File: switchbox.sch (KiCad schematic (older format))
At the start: 3 parts

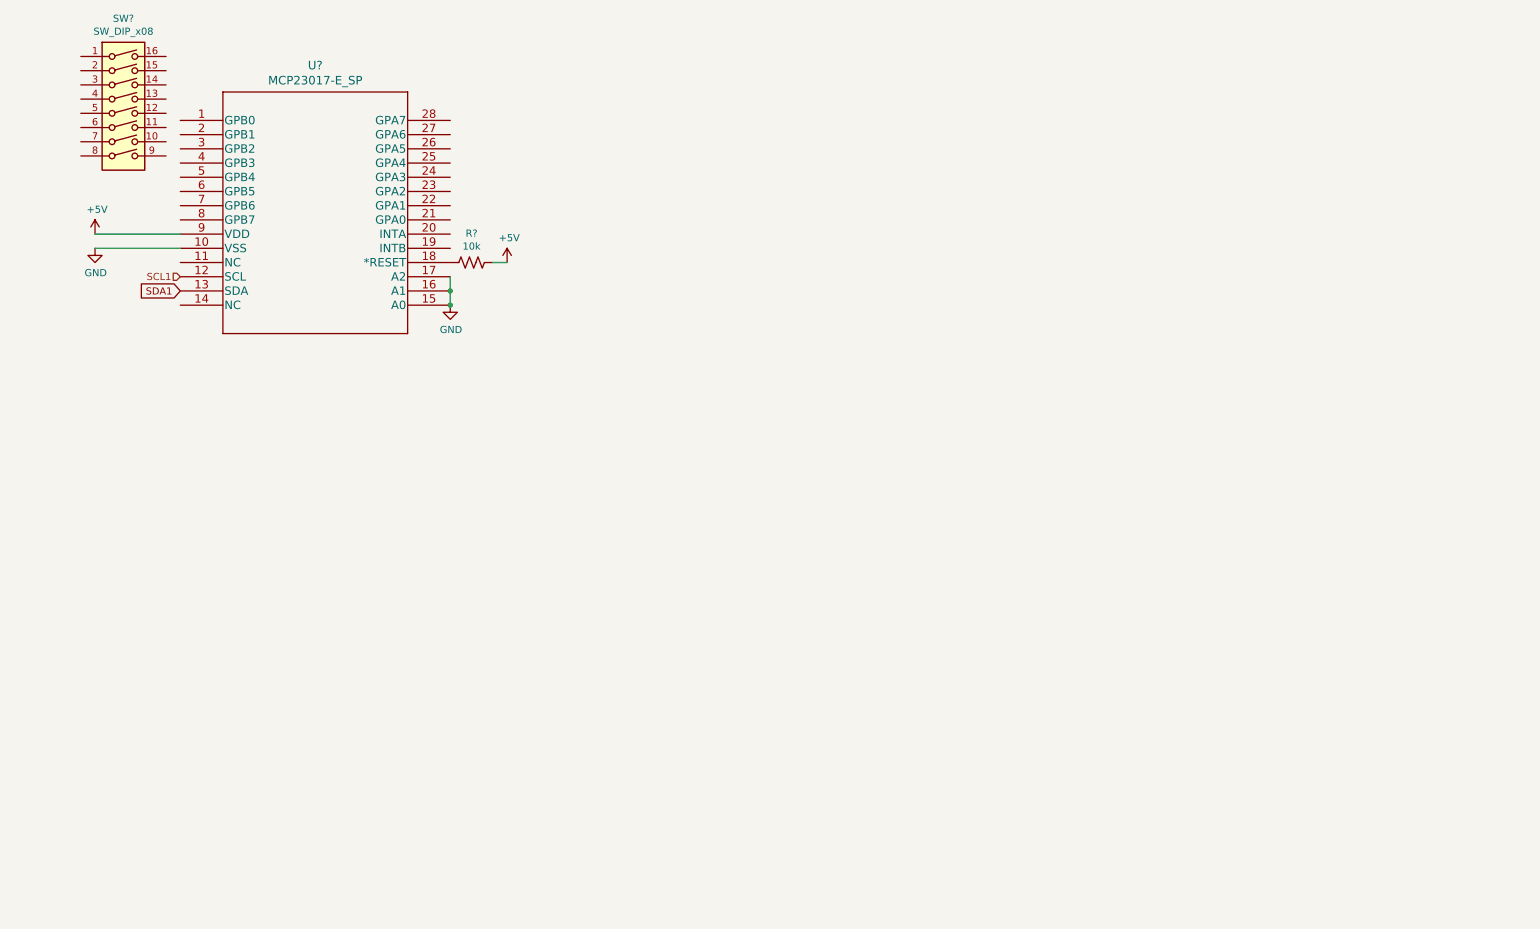
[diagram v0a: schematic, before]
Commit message: Switchbox Schematic Created
The nested schematic for the switchbox no exists using the 12V battery, LM2596 buck converter, and the MPC23017 I/O expander.
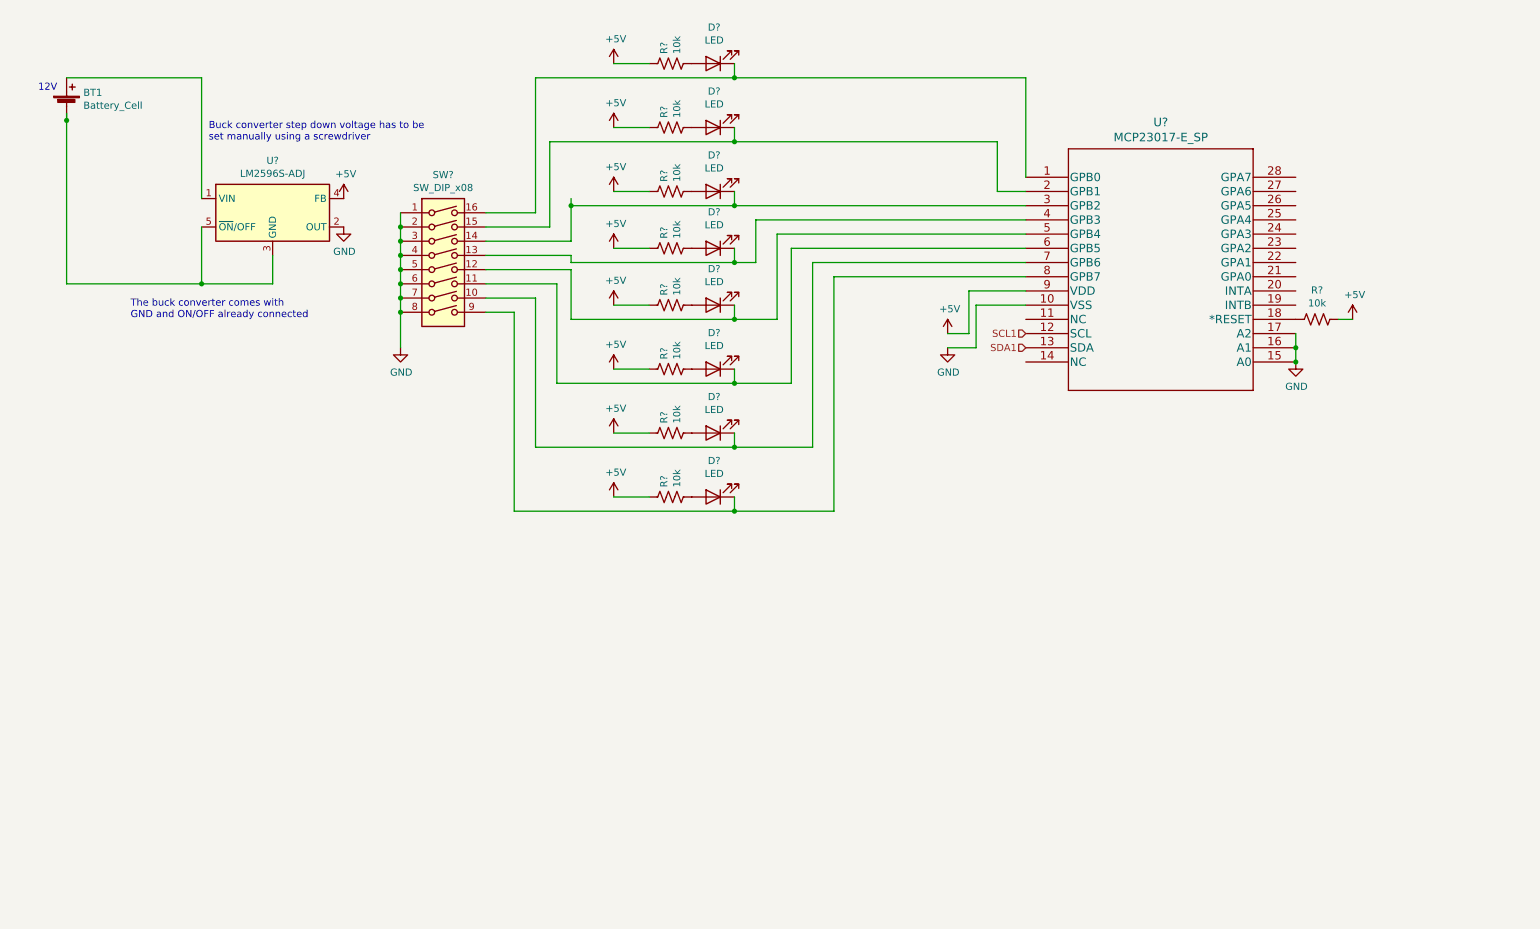
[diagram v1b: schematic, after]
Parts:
- added BT1: Battery_Cell, symbol Device:Battery_Cell
- added D? (x8): LED, symbol Device:LED
- added R? (x8): 10k, symbol Device:R_US
- added U?: LM2596S-ADJ, Package_TO_SOT_SMD:TO-263-5_TabPin3, symbol Regulator_Switching:LM2596S-ADJ
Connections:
- net +5V: now also R?.1, R?.1, R?.1, R?.1, R?.1, R?.1, R?.1, R?.1, U?.4 (FB)
- net GND: now also SW?.1, SW?.2, SW?.3, SW?.4, SW?.5, SW?.6, SW?.7, SW?.8, U?.2 (OUT)
- net at U?.1 (GPB0): now also SW?.16, D?.1 (K)
- net at U?.2 (GPB1): now also SW?.15, D?.1 (K)
- net at U?.3 (GPB2): now also SW?.14, D?.1 (K)
- net at U?.4 (GPB3): now also SW?.13, D?.1 (K)
- net at U?.5 (GPB4): now also SW?.12, D?.1 (K)
- net at U?.6 (GPB5): now also SW?.11, D?.1 (K)
- net at U?.7 (GPB6): now also SW?.10, D?.1 (K)
- net at U?.8 (GPB7): now also SW?.9, D?.1 (K)
- new net: BT1.1 (+), U?.1 (VIN)
- new net: BT1.2 (-), U?.3 (GND), U?.5 (~ON~/OFF)
- new net: D?.2 (A), R?.2 (x8)
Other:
- note added: "12V"
- note added: "Buck converter step down voltage has to be\nset manually using a screwdriver"
- note added: "The buck converter comes with\nGND and ON/OFF already connected"
- moved on the sheet: R?, SW?, U?

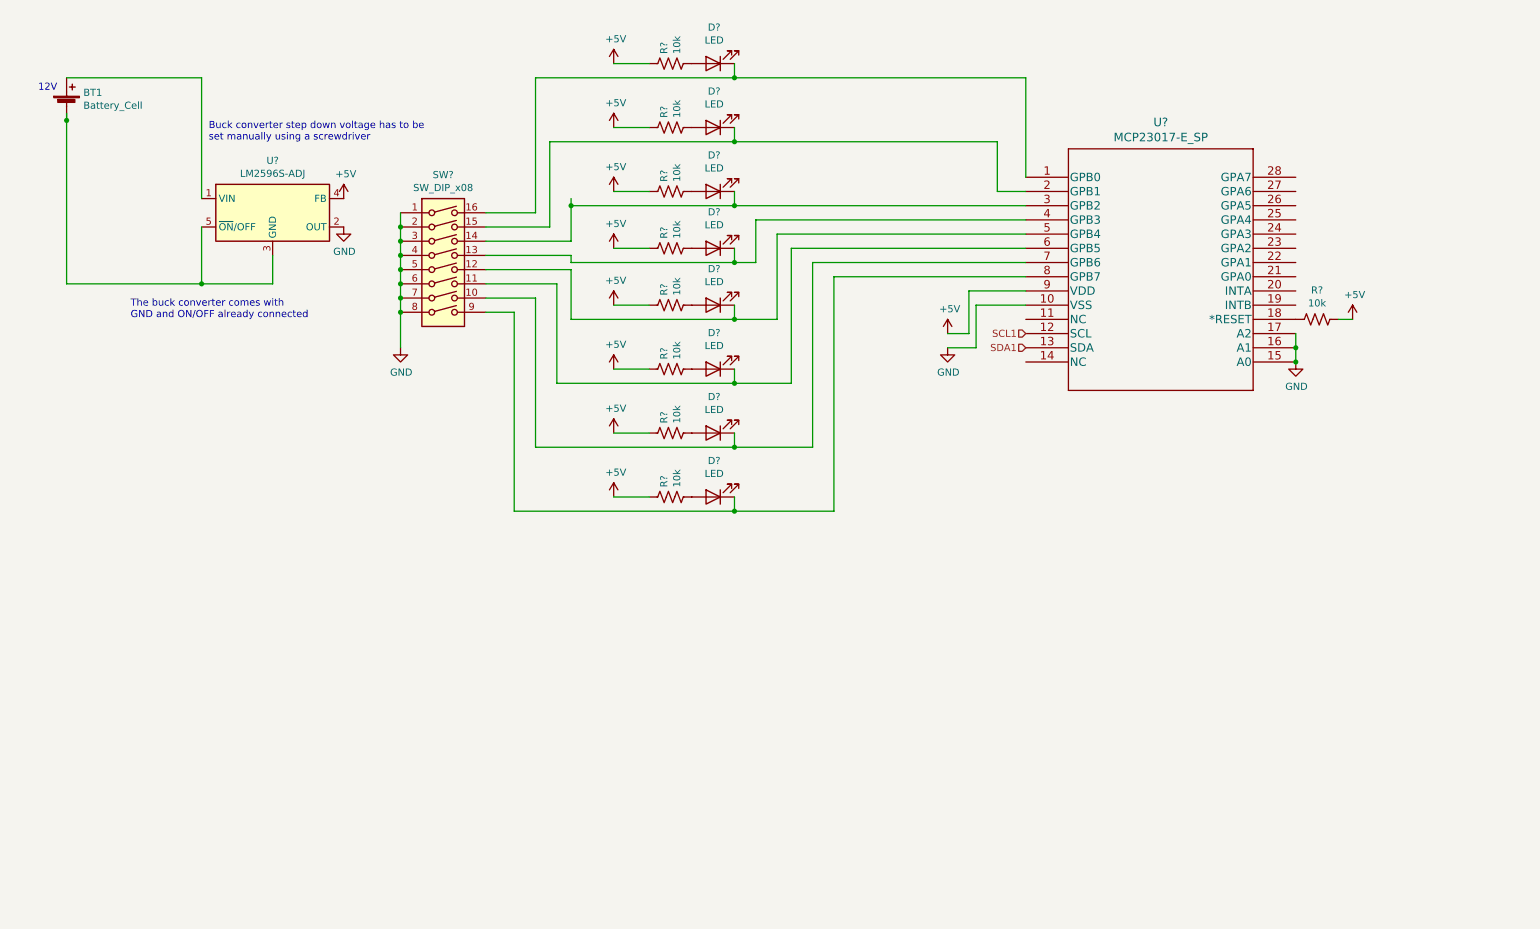
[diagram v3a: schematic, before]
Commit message: Added Capability for 16 Actuators
The prevous 8 switches was doubled so that 16 switches now plug into the MPC23017 for up to 16 actuations remote side.
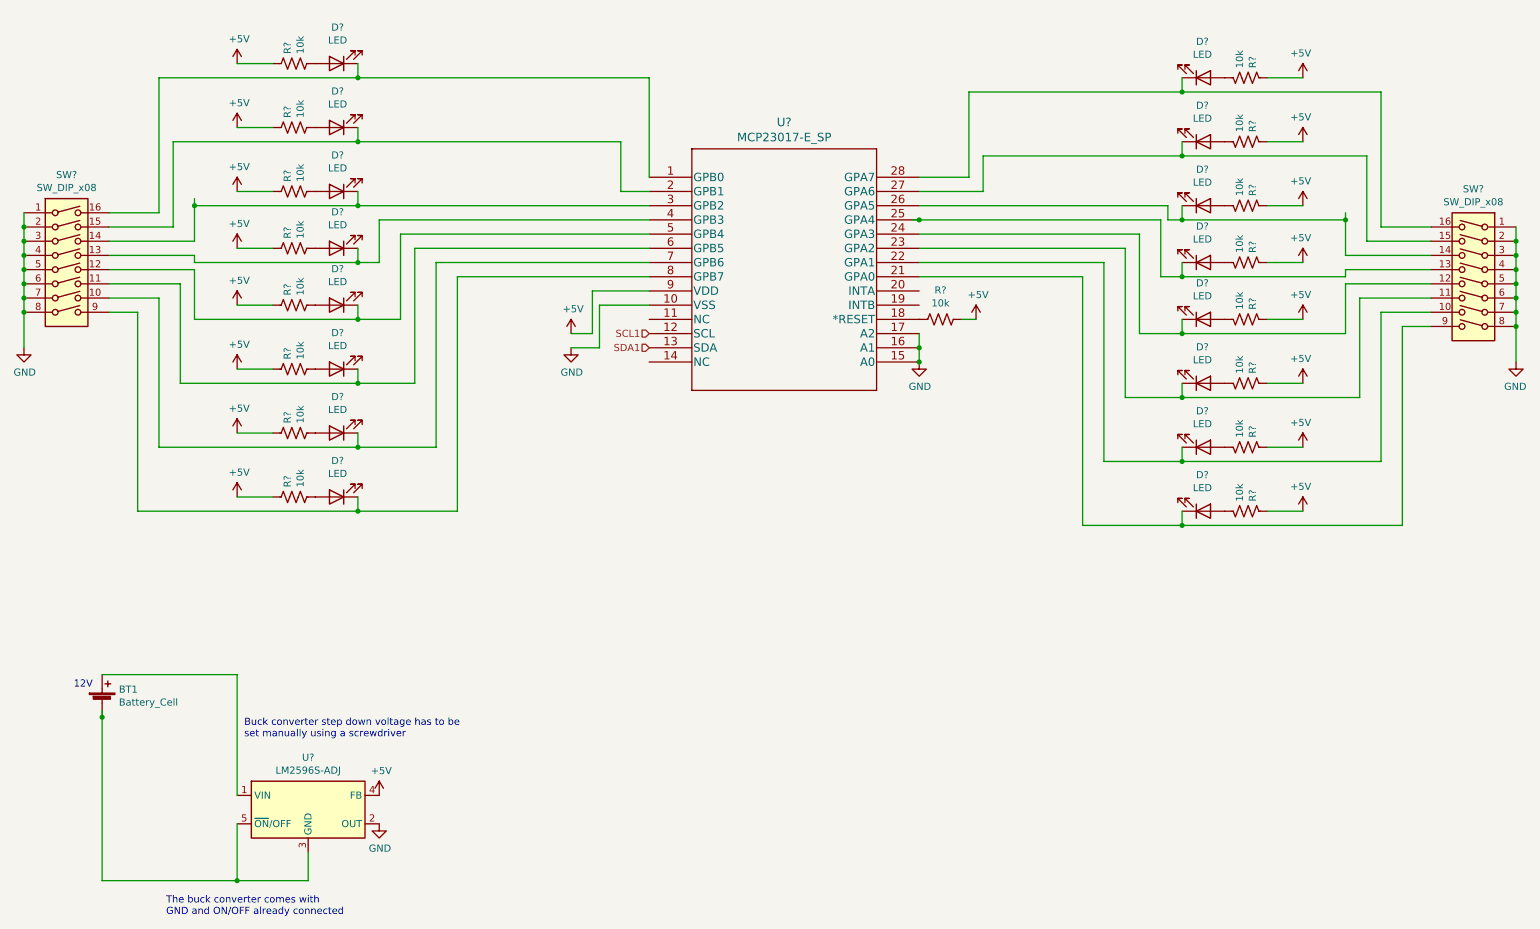
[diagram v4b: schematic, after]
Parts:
- added D? (x8): LED, symbol Device:LED
- added R? (x8): 10k, symbol Device:R_US
- added SW?: SW_DIP_x08, symbol Switch:SW_DIP_x08
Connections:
- net +5V: now also R?.1, R?.1, R?.1, R?.1, R?.1, R?.1, R?.1, R?.1
- net GND: now also SW?.1, SW?.2, SW?.3, SW?.4, SW?.5, SW?.6, SW?.7, SW?.8
- net at U?.21 (GPA0): now also D?.1 (K), SW?.9
- net at U?.22 (GPA1): now also D?.1 (K), SW?.10
- net at U?.23 (GPA2): now also D?.1 (K), SW?.11
- net at U?.24 (GPA3): now also D?.1 (K), SW?.12
- net at U?.25 (GPA4): now also D?.1 (K), SW?.13
- net at U?.26 (GPA5): now also D?.1 (K), SW?.14
- net at U?.27 (GPA6): now also D?.1 (K), SW?.15
- net at U?.28 (GPA7): now also D?.1 (K), SW?.16
- new net: D?.2 (A), R?.2 (x8)
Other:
- moved on the sheet: BT1, D?, R?, SW?, U?

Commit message: Added Refrences
Used the Netlist function in KiCAD to automatically label all the components.
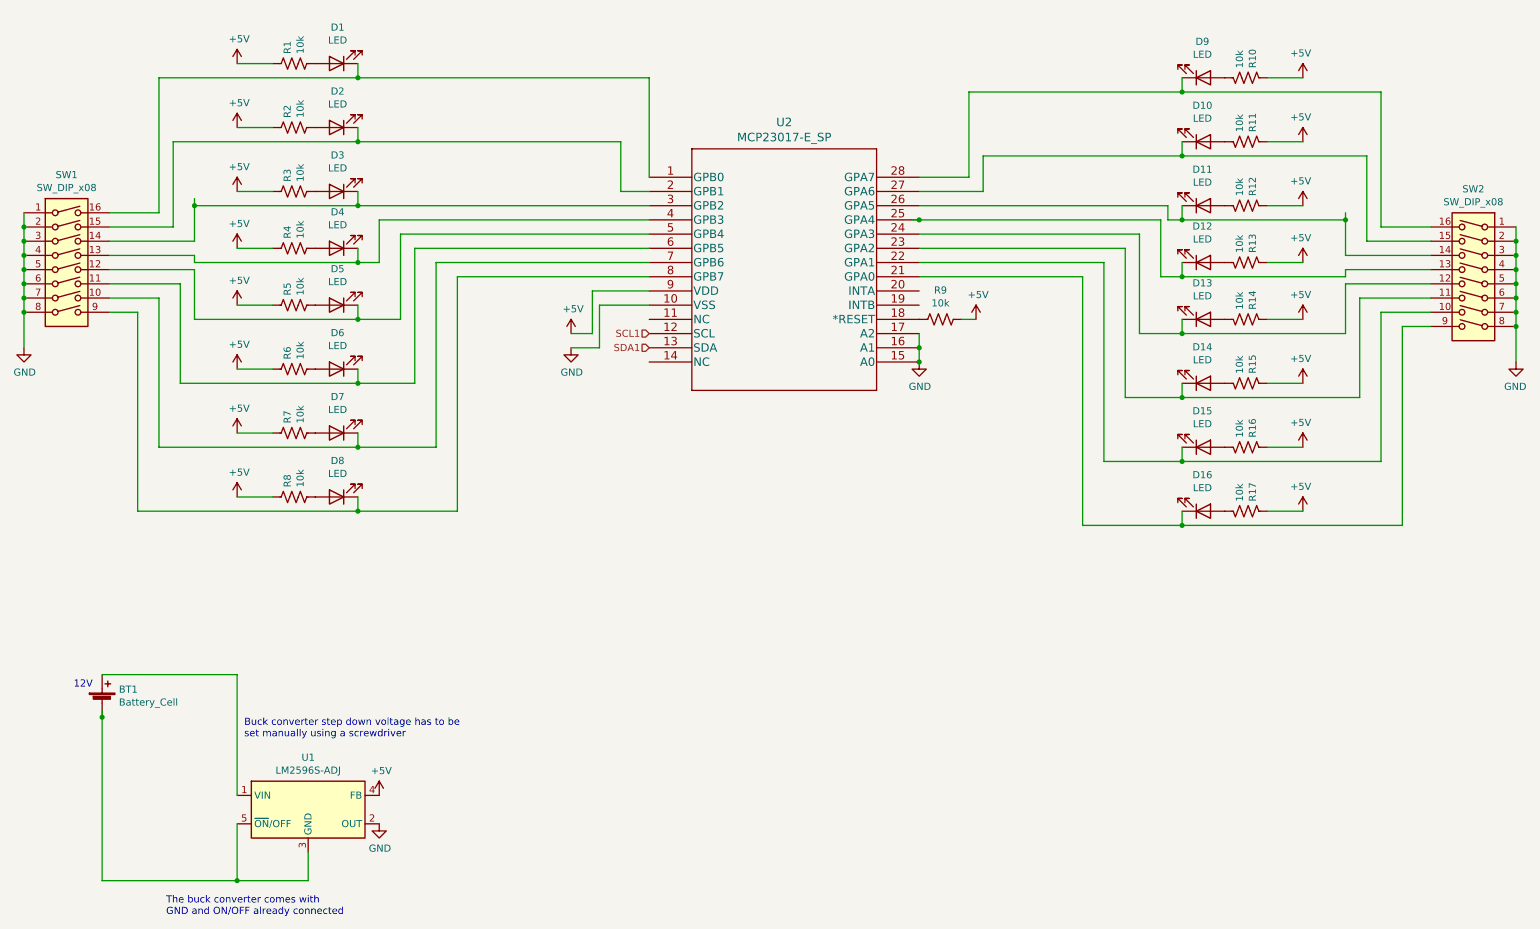
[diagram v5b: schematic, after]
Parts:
- gave numbers to parts that had none: 37

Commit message: publish jeff review
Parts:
- removed BT1: Battery_Cell, symbol Device:Battery_Cell
- removed U1: LM2596S-ADJ, Package_TO_SOT_SMD:TO-263-5_TabPin3, symbol Regulator_Switching:LM2596S-ADJ
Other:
- note removed: "12V"
- note removed: "Buck converter step down voltage has to be\nset manually using a screwdriver"
- note removed: "The buck converter comes with\nGND and ON/OFF already connected"
